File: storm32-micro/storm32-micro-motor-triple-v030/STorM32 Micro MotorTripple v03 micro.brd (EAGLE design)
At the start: 26 x 26 mm, 32 parts, among them IC1 STM32F10XTXU6, IC3 DRV8839, IC4 DRV8839, IC5 DRV8839, IC6 DRV8839, IC7 DRV8839, Q1 RESONATORSMD

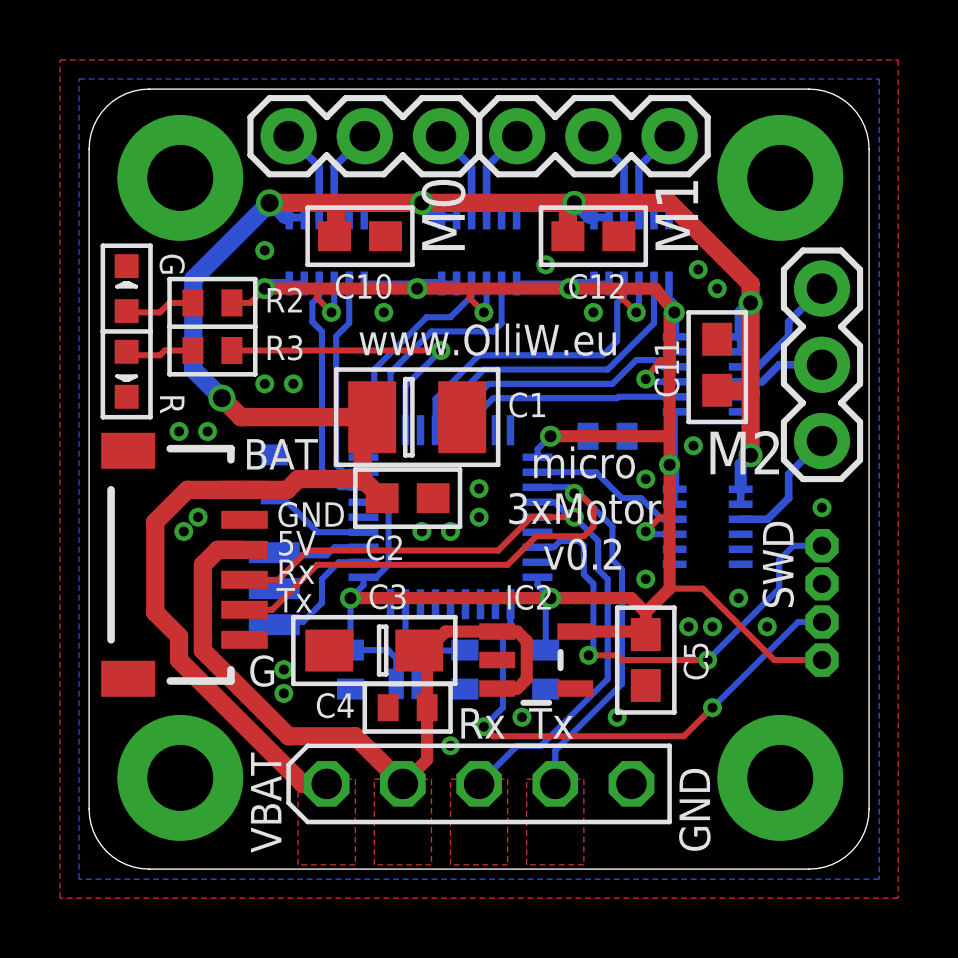
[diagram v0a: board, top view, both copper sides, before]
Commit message: release STorM32 Micro Motor Triple Board v0.30
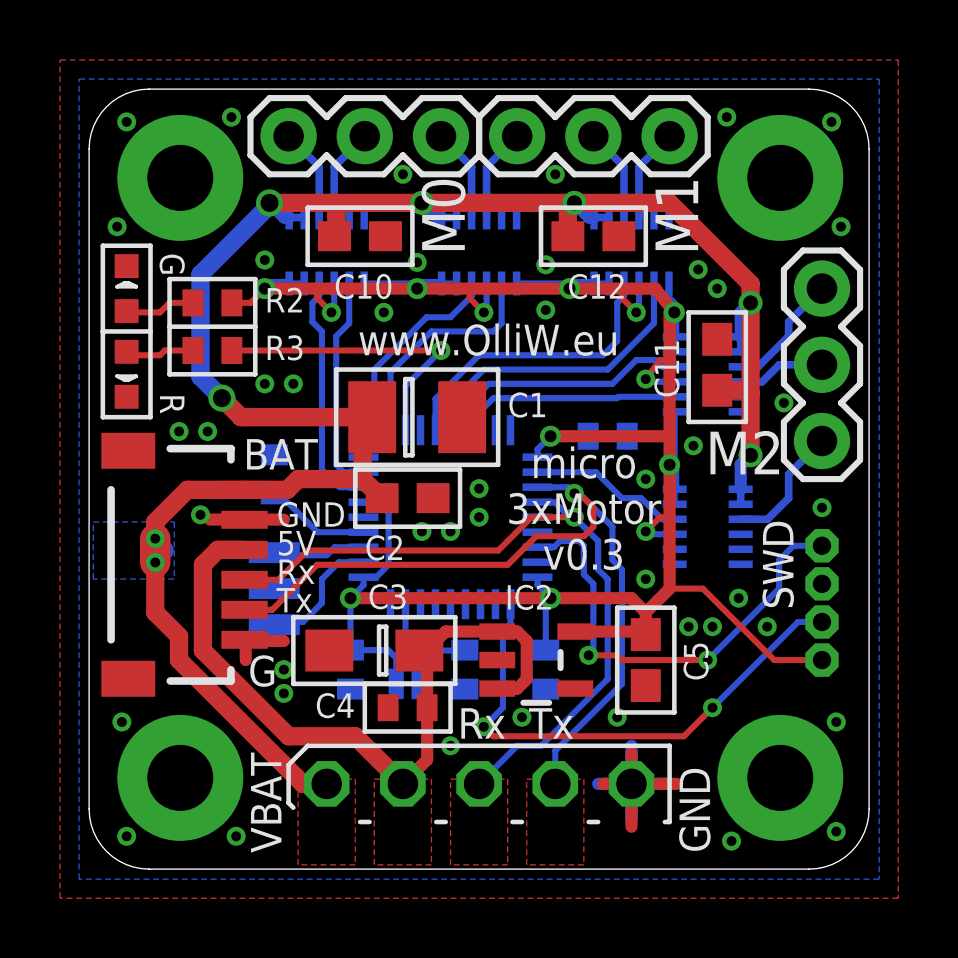
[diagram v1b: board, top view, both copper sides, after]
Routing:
- net GND: track 0.00 -> 14.8 mm, vias 33 -> 48
- net VCCG: track 69.7 -> 70.8 mm, vias 6 -> 8
- added copper zone on layer 16, net VCCG
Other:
- board text added: "+"
- board text added: "-"
- board text added: "micro 3xMotor v0.3"
- board text removed: "micro 3xMotor v0.2"
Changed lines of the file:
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@@
 <wire x1="28.24" y1="26.24" x2="28.24" y2="4.24" width="0" layer="20"/>
 <text x="18.25625" y="25.479375" size="1.016" layer="26" font="vector" ratio="15" rot="SMR180">M1</text>
-<text x="8.651875" y="6.270625" size="1.016" layer="26" font="vector" ratio="15" rot="SMR270">VBAT</text>
+<text x="5.318125" y="12.22375" size="1.6764" layer="26" font="vector" ratio="20" rot="SMR90">+</text>
 <text x="22.5425" y="22.70125" size="1.4224" layer="25" font="vector" ratio="15" rot="SR90">M1</text>
 <text x="13.49375" y="6.6675" size="1.016" layer="26" font="vector" ratio="15" rot="SMR0">BL</text>
@@
 <wire x1="10.16" y1="10.31875" x2="10.16" y2="7.46125" width="0.1524" layer="22"/>
 <wire x1="11.7475" y1="10.31875" x2="11.7475" y2="7.46125" width="0.1524" layer="22"/>
-<circle x="8.09625" y="23.733125" radius="0.254" width="0.254" layer="22"/>
+<circle x="8.255" y="23.891875" radius="0.254" width="0.254" layer="22"/>
 <circle x="11.27125" y="10.95375" radius="0.254" width="0.254" layer="22"/>
 <circle x="23.891875" y="20.716875" radius="0.254" width="0.254" layer="22"/>
@@
 <wire x1="8.89" y1="5.715" x2="8.89" y2="4.445" width="0.1524" layer="21"/>
 <wire x1="21.59" y1="6.35" x2="21.59" y2="3.81" width="0.1524" layer="21"/>
-<wire x1="8.89" y1="4.445" x2="9.525" y2="3.81" width="0.1524" layer="21"/>
 <wire x1="8.89" y1="5.715" x2="9.525" y2="6.35" width="0.1524" layer="21"/>
 <wire x1="9.525" y1="6.35" x2="21.59" y2="6.35" width="0.1524" layer="21"/>
-<wire x1="9.525" y1="3.81" x2="21.59" y2="3.81" width="0.1524" layer="21"/>
+<wire x1="21.43125" y1="3.81" x2="21.59" y2="3.81" width="0.1524" layer="21"/>
 <text x="18.7325" y="12.22375" size="1.016" layer="25" font="vector" ratio="20" rot="SR0" align="bottom-center">micro
 3xMotor
-v0.2</text>
+v0.3</text>
 <rectangle x1="12.54125" y1="12.22375" x2="16.03375" y2="15.71625" layer="30"/>
 <rectangle x1="12.85875" y1="12.54125" x2="15.71625" y2="15.39875" layer="32"/>
@@
 <rectangle x1="16.1528125" y1="2.6590625" x2="19.4071875" y2="4.7228125" layer="29" rot="R270"/>
 <rectangle x1="18.6928125" y1="2.6590625" x2="21.9471875" y2="4.7228125" layer="29" rot="R270"/>
-<text x="3.96875" y="15.24" size="1.016" layer="26" font="vector" ratio="20" rot="SMR270" align="bottom-center">www.OlliW.eu</text>
+<text x="3.81" y="18.7325" size="0.9652" layer="26" font="vector" ratio="20" rot="SMR270" align="bottom-center">www.OlliW.eu</text>
+<rectangle x1="1.905" y1="11.826875" x2="5.159375" y2="13.890625" layer="30"/>
+<rectangle x1="1.905" y1="9.128125" x2="5.159375" y2="11.191875" layer="30"/>
+<text x="5.318125" y="9.525" size="1.6764" layer="26" font="vector" ratio="20" rot="SMR90">-</text>
+<text x="8.651875" y="6.270625" size="0.9906" layer="26" font="vector" ratio="15" rot="SMR270">VBAT</text>
+<wire x1="18.89125" y1="3.81" x2="19.20875" y2="3.81" width="0.1524" layer="21"/>
+<wire x1="16.35125" y1="3.81" x2="16.66875" y2="3.81" width="0.1524" layer="21"/>
+<wire x1="13.81125" y1="3.81" x2="14.12875" y2="3.81" width="0.1524" layer="21"/>
+<wire x1="11.27125" y1="3.81" x2="11.58875" y2="3.81" width="0.1524" layer="21"/>
+<circle x="13.335" y="23.891875" radius="0.254" width="0.254" layer="22"/>
+<circle x="18.415" y="23.891875" radius="0.254" width="0.254" layer="22"/>
+<wire x1="8.89" y1="4.445" x2="9.04875" y2="4.28625" width="0.1524" layer="21"/>
 </plain>
 <attributes>
@@
 </element>
 <element name="Q1" library="# SparkFun2" package="RESONATOR-SMD" value="RESONATORSMD" x="8.41375" y="11.58875" smashed="yes" rot="MR90">
-<attribute name="NAME" x="7.08025" y="11.27125" size="0.8128" layer="26" font="vector" rot="MR0"/>
+<attribute name="NAME" x="10.31875" y="12.16025" size="0.8128" layer="26" font="vector" rot="SMR270"/>
 </element>
 <element name="LED1" library="led" package="CHIPLED_0603" value="red" x="3.4925" y="21.59" smashed="yes">
@@
 <contactref element="IC7" pad="5"/>
 <contactref element="C11" pad="2"/>
-<via x="5.87375" y="13.97" extent="1-16" drill="0.3302"/>
+<via x="5.953125" y="14.049375" extent="1-16" drill="0.3302"/>
 <via x="12.065" y="20.79625" extent="1-16" drill="0.3302"/>
-<via x="19.05" y="20.79625" extent="1-16" drill="0.3302"/>
-<via x="8.09625" y="22.86" extent="1-16" drill="0.3302"/>
+<via x="17.4625" y="20.875625" extent="1-16" drill="0.3302"/>
+<via x="8.09625" y="22.5425" extent="1-16" drill="0.3302"/>
 <via x="23.01875" y="10.31875" extent="1-16" drill="0.3302"/>
 <via x="24.844375" y="10.31875" extent="1-16" drill="0.3302"/>
@@
 <via x="22.225" y="10.31875" extent="1-16" drill="0.3302"/>
 <via x="20.79625" y="11.90625" extent="1-16" drill="0.3302"/>
-<via x="5.3975" y="13.49375" extent="1-16" drill="0.3302"/>
 <via x="8.09625" y="18.415" extent="1-16" drill="0.3302"/>
 <via x="9.04875" y="18.415" extent="1-16" drill="0.3302"/>
@@
 <via x="17.4625" y="22.38375" extent="1-16" drill="0.3302"/>
 <via x="23.891875" y="11.27125" extent="1-16" drill="0.3302"/>
+<via x="3.175" y="23.65375" extent="1-16" drill="0.3302"/>
+<via x="3.4925" y="27.14625" extent="1-16" drill="0.3302"/>
+<via x="6.985" y="27.305" extent="1-16" drill="0.3302"/>
+<via x="26.9875" y="27.14625" extent="1-16" drill="0.3302"/>
+<via x="23.495" y="27.305" extent="1-16" drill="0.3302"/>
+<via x="27.305" y="23.65375" extent="1-16" drill="0.3302"/>
+<via x="27.14625" y="3.4925" extent="1-16" drill="0.3302"/>
+<via x="27.14625" y="7.14375" extent="1-16" drill="0.3302"/>
+<via x="23.65375" y="3.175" extent="1-16" drill="0.3302"/>
+<via x="3.4925" y="3.33375" extent="1-16" drill="0.3302"/>
+<via x="3.33375" y="7.14375" extent="1-16" drill="0.3302"/>
+<via x="7.14375" y="3.33375" extent="1-16" drill="0.3302"/>
+<via x="17.78" y="25.4" extent="1-16" drill="0.3302"/>
+<via x="12.7" y="25.4" extent="1-16" drill="0.3302"/>
+<via x="25.4" y="17.78" extent="1-16" drill="0.3302"/>
+<wire x1="6.270625" y1="13.890625" x2="8.73125" y2="13.890625" width="0.4064" layer="1"/>
+<wire x1="6.905625" y1="9.8425" x2="7.46125" y2="9.8425" width="0.4064" layer="1"/>
+<wire x1="7.46125" y1="9.8425" x2="8.73125" y2="9.8425" width="0.4064" layer="1"/>
+<wire x1="7.46125" y1="9.2075" x2="7.46125" y2="9.8425" width="0.4064" layer="1"/>
+<wire x1="21.828125" y1="5.08" x2="19.3675" y2="5.08" width="0.4064" layer="1"/>
+<wire x1="20.32" y1="6.111875" x2="20.32" y2="3.65125" width="0.4064" layer="1"/>
+<wire x1="21.669375" y1="5.08" x2="19.20875" y2="5.08" width="0.4064" layer="16"/>
+<wire x1="20.32" y1="6.35" x2="20.32" y2="3.889375" width="0.4064" layer="16"/>
+<via x="13.17625" y="22.463125" extent="1-16" drill="0.3302"/>
 </signal>
 <signal name="N$2">
@@
 <wire x1="11.35875" y1="15.225" x2="12.00875" y2="14.605" width="0.6096" layer="1"/>
 <contactref element="U$1" pad="1"/>
-<wire x1="10.16" y1="5.08" x2="9.36625" y2="5.08" width="0.6096" layer="1"/>
-<wire x1="9.36625" y1="5.08" x2="5.23875" y2="9.2075" width="0.6096" layer="1"/>
 <wire x1="5.23875" y1="9.2075" x2="5.23875" y2="10.00125" width="0.6096" layer="1"/>
 <wire x1="5.23875" y1="10.00125" x2="4.445" y2="10.795" width="0.6096" layer="1"/>
-<wire x1="4.445" y1="10.795" x2="4.445" y2="13.81125" width="0.6096" layer="1"/>
+<wire x1="4.445" y1="10.795" x2="4.445" y2="12.461875" width="0.6096" layer="1"/>
+<wire x1="4.445" y1="12.461875" x2="4.445" y2="13.81125" width="0.6096" layer="1"/>
 <wire x1="4.445" y1="13.81125" x2="5.51625" y2="14.8825" width="0.6096" layer="1"/>
 <wire x1="7.42" y1="14.8825" x2="5.51625" y2="14.8825" width="0.6096" layer="1"/>
@@
 <wire x1="7.3025" y1="17.30375" x2="6.6675" y2="17.93875" width="0.6096" layer="1"/>
 <via x="6.6675" y="17.93875" extent="1-16" drill="0.6"/>
-<wire x1="6.6675" y1="17.93875" x2="5.715" y2="18.89125" width="0.6096" layer="16"/>
-<wire x1="5.715" y1="18.89125" x2="5.715" y2="21.9075" width="0.6096" layer="16"/>
-<wire x1="5.715" y1="21.9075" x2="8.255" y2="24.4475" width="0.6096" layer="16"/>
+<wire x1="6.6675" y1="17.93875" x2="5.953125" y2="18.653125" width="0.6096" layer="16"/>
+<wire x1="5.953125" y1="18.653125" x2="5.953125" y2="22.06625" width="0.6096" layer="16"/>
+<wire x1="5.953125" y1="22.06625" x2="8.255" y2="24.368125" width="0.6096" layer="16"/>
+<wire x1="8.255" y1="24.368125" x2="8.255" y2="24.4475" width="0.6096" layer="16"/>
 <wire x1="10.42125" y1="23.33625" x2="10.4775" y2="23.33625" width="0.2032" layer="1"/>
 <wire x1="10.4775" y1="23.33625" x2="10.4775" y2="24.4475" width="0.6096" layer="1"/>
@@
 <vertex x="11.1125" y="2.38125"/>
 </polygon>
+<wire x1="4.445" y1="13.255625" x2="4.7625" y2="12.85875" width="0.6096" layer="16"/>
+<wire x1="5.23875" y1="9.2075" x2="9.36625" y2="5.08" width="0.6096" layer="1"/>
+<wire x1="9.36625" y1="5.08" x2="10.16" y2="5.08" width="0.6096" layer="1"/>
+<polygon width="0.1524" layer="16" isolate="0.3048">
+<vertex x="2.38125" y="13.81125"/>
+<vertex x="5.08" y="13.81125"/>
+<vertex x="5.08" y="11.90625"/>
+<vertex x="2.38125" y="11.90625"/>
+</polygon>
+<via x="4.445" y="13.255625" extent="1-16" drill="0.3302"/>
+<via x="4.445" y="12.461875" extent="1-16" drill="0.3302"/>
+<wire x1="4.445" y1="13.255625" x2="4.445" y2="12.461875" width="1.016" layer="1"/>
 </signal>
 <signal name="N$13">
